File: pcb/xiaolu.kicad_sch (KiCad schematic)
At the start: 35 parts, among them J1 Conn_01x04_Male, J2 TRRS, SW1 SW_Push, SW10 SW_Push, SW11 SW_Push, SW12 SW_Push, SW13 SW_Push, SW14 SW_Push, SW15 SW_Push, SW16 SW_Push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

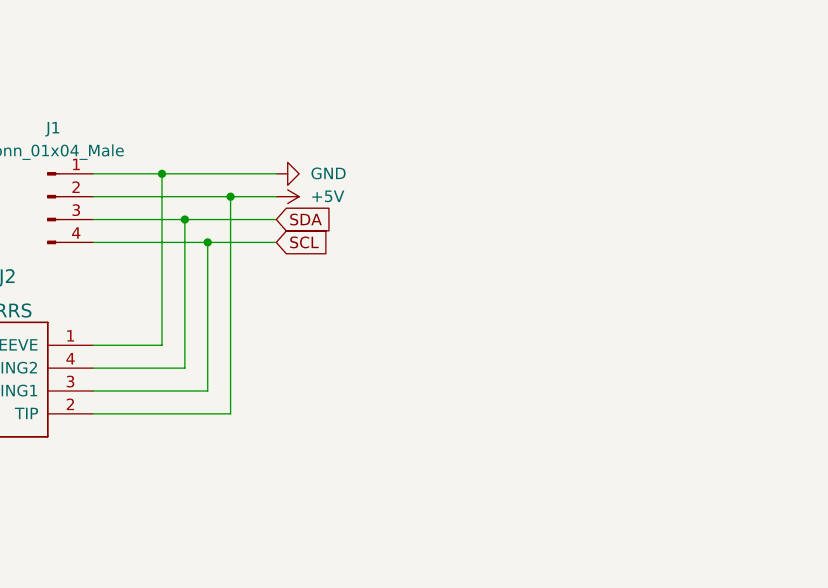
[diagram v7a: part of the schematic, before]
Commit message: add optional pull-up registers to I2C SDA/SCL
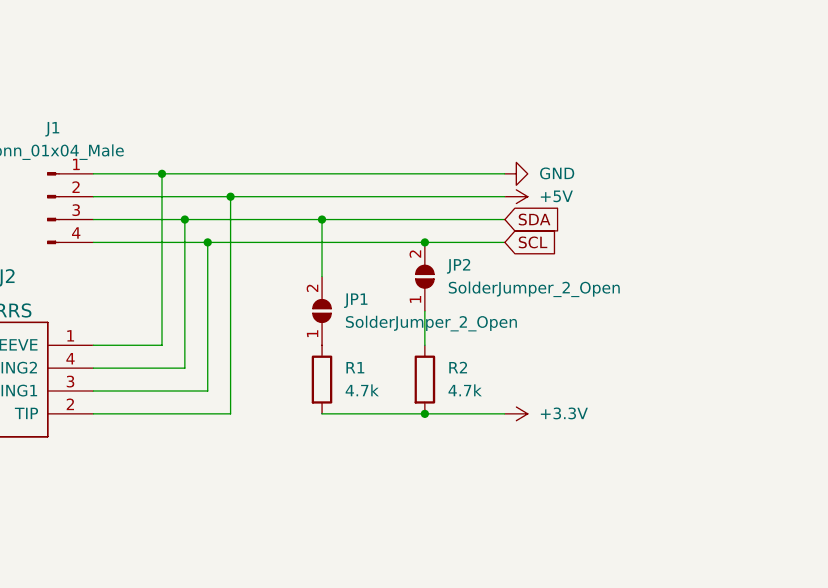
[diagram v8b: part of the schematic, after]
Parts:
- added JP1, JP2: SolderJumper_2_Open, Jumper:SolderJumper-2_P1.3mm_Open_RoundedPad1.0x1.5mm, symbol Jumper:SolderJumper_2_Open
- added R1, R2: 4.7k, Resistor_SMD:R_0402_1005Metric, symbol Device:R
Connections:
- net +3.3V: now also R1.2, R2.2
- net SCL: now also JP2.2 (B)
- net SDA: now also JP1.2 (B)
- new net: JP1.1 (A), R1.1
- new net: JP2.1 (A), R2.1
